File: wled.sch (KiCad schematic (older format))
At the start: 18 parts, among them J1 PROGRAM_HEADER, J2 LED0, J3 QWIIC, J4 POWER, Q1 S8050, Q2 S8050, U1 ESP-12F, U2 AMS1117-3.3

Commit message: fix 0603 components
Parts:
- C1, C2: footprint Capacitor_SMD:C_0201_0603Metric -> Capacitor_SMD:C_0603_1608Metric
- D2: footprint LED_SMD:LED_0201_0603Metric -> LED_SMD:LED_0603_1608Metric
- R1, R2: footprint Resistor_SMD:R_0201_0603Metric -> Resistor_SMD:R_0603_1608Metric
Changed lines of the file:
@@
 F 0 "R1" V 7493 2050 50  0000 C CNN
 F 1 "12k" V 7584 2050 50  0000 C CNN
-F 2 "Resistor_SMD:R_0201_0603Metric" V 7630 2050 50  0001 C CNN
+F 2 "Resistor_SMD:R_0603_1608Metric" V 7630 2050 50  0001 C CNN
 F 3 "~" H 7700 2050 50  0001 C CNN
 F 4 "C22790" H 7700 2050 50  0001 C CNN "JCSC"
@@
 F 0 "R2" V 7493 3200 50  0000 C CNN
 F 1 "12k" V 7584 3200 50  0000 C CNN
-F 2 "Resistor_SMD:R_0201_0603Metric" V 7630 3200 50  0001 C CNN
+F 2 "Resistor_SMD:R_0603_1608Metric" V 7630 3200 50  0001 C CNN
 F 3 "~" H 7700 3200 50  0001 C CNN
 F 4 "C22790" H 7700 3200 50  0001 C CNN "JCSC"
@@
 F 0 "C1" H 3815 4896 50  0000 L CNN
 F 1 "10uF" H 3815 4805 50  0000 L CNN
-F 2 "Capacitor_SMD:C_0201_0603Metric" H 3738 4700 50  0001 C CNN
+F 2 "Capacitor_SMD:C_0603_1608Metric" H 3738 4700 50  0001 C CNN
 F 3 "~" H 3700 4850 50  0001 C CNN
 F 4 "C19702" H 3700 4850 50  0001 C CNN "JCSC"
@@
 F 0 "C2" H 4765 4946 50  0000 L CNN
 F 1 "10uF" H 4765 4855 50  0000 L CNN
-F 2 "Capacitor_SMD:C_0201_0603Metric" H 4688 4750 50  0001 C CNN
+F 2 "Capacitor_SMD:C_0603_1608Metric" H 4688 4750 50  0001 C CNN
 F 3 "~" H 4650 4900 50  0001 C CNN
 F 4 "C19702" H 4650 4900 50  0001 C CNN "JCSC"
@@
 F 0 "D2" H 3443 5695 50  0000 C CNN
 F 1 "LED" H 3443 5786 50  0000 C CNN
-F 2 "LED_SMD:LED_0201_0603Metric" H 3450 5950 50  0001 C CNN
+F 2 "LED_SMD:LED_0603_1608Metric" H 3450 5950 50  0001 C CNN
 F 3 "~" H 3450 5950 50  0001 C CNN
 F 4 "C2286" H 3450 5950 50  0001 C CNN "JCSC"

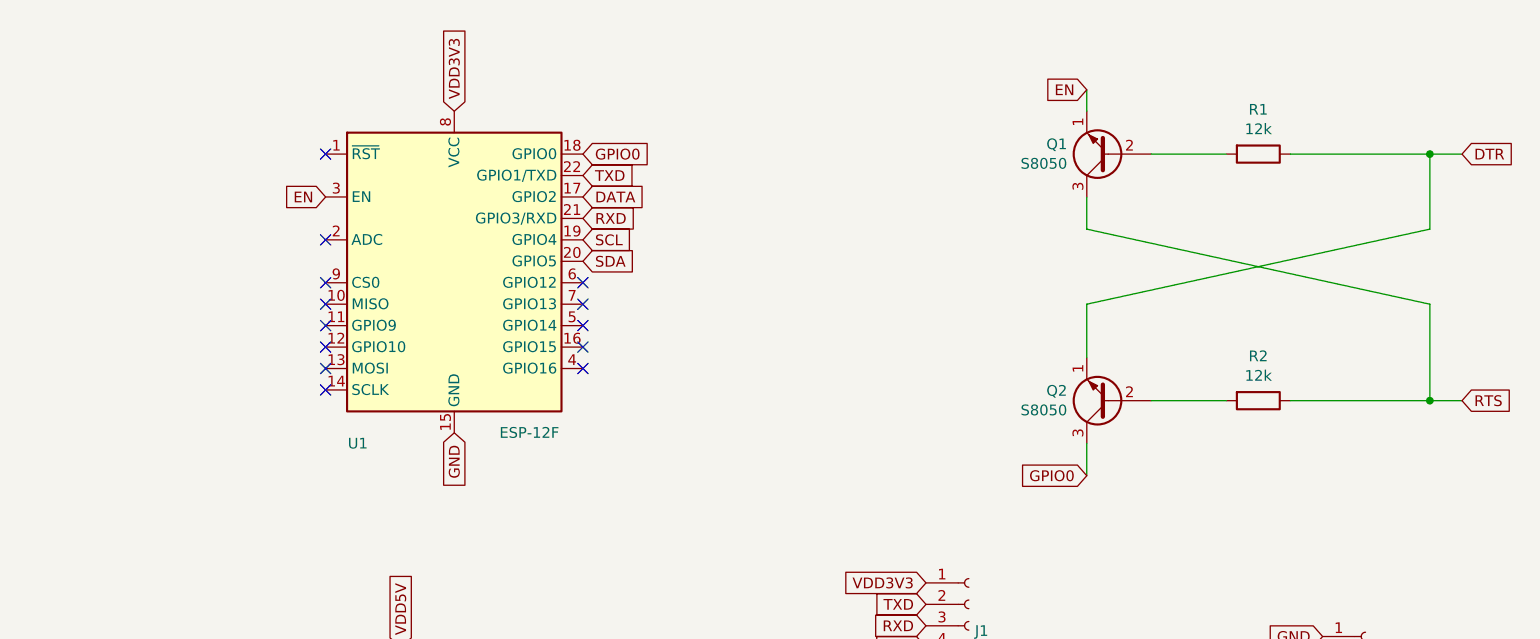
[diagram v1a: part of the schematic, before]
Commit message: updated parts/placements
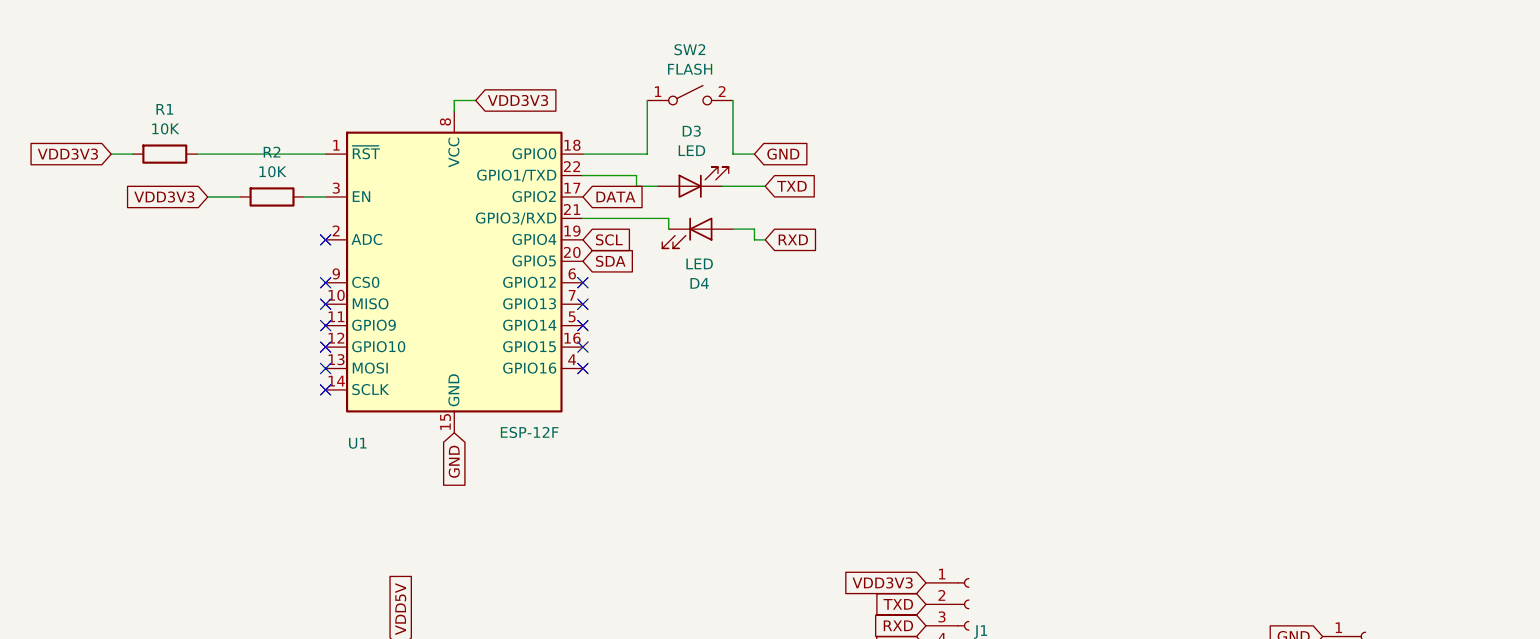
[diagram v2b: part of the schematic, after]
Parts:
- removed Q1, Q2: S8050, Package_TO_SOT_SMD:SOT-23, symbol Transistor_BJT:S8050
- added D3, D4: LED, LED_SMD:LED_0603_1608Metric, symbol Device:LED
- added SW2: FLASH, Button_Switch_SMD:SW_SPST_B3S-1000, symbol Switch:SW_SPST
- J1: footprint Connector_PinSocket_2.54mm:PinSocket_1x06_P2.54mm_Vertical -> Connector_JST:JST_XH_B6B-XH-A_1x06_P2.50mm_Vertical
- J4: footprint Connector_JST:JST_PH_B2B-PH-K_1x02_P2.00mm_Vertical -> Connector_JST:JST_XH_B2B-XH-A_1x02_P2.50mm_Vertical
- R1, R2: value 12k -> 10K; footprint Resistor_SMD:R_0603_1608Metric -> Resistor_SMD:R_0603_1608Metric_Pad0.98x0.95mm_HandSolder; JCSC C22790 -> (none); LCSC Part C22790 -> (none)
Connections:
- net DTR: no longer R1.1
- net GND: now also SW2.2 (B)
- net RTS: no longer R2.1
- net RXD: now also D4.2 (A); no longer U1.21 (GPIO3/RXD)
- net TXD: now also D3.1 (K); no longer U1.22 (GPIO1/TXD)
- net VDD3V3: now also R1.2, R2.2
- net at U1.1 (~RST): now also R1.1
- net EN: no longer names the net of U1.3 (EN)
- net EN: now also R2.1
- net GPIO0: no longer names the net of U1.18 (GPIO0)
- net GPIO0: now also SW2.1 (A)
- new net: D4.1 (K), U1.21 (GPIO3/RXD)
- new net: D3.2 (A), U1.22 (GPIO1/TXD)
- no-connect marks 13 -> 12
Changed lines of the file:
@@
 Comment4 ""
 $EndDescr
-$Comp
-L RF_Module:ESP-12F U1
-U 1 1 605E2E75
-P 3950 2650
-F 0 "U1" H 3500 1900 50  0000 C CNN
-F 1 "ESP-12F" H 4300 1950 50  0000 C CNN
-F 2 "RF_Module:ESP-12E" H 3950 2650 50  0001 C CNN
-F 3 "http://wiki.ai-thinker.com/_media/esp8266/esp8266_series_modules_user_manual_v1.1.pdf" H 3600 2750 50  0001 C CNN
-F 4 "C82891" H 3950 2650 50  0001 C CNN "JCSC"
-F 5 "C82891" H 3950 2650 50  0001 C CNN "LCSC Part"
-	1    3950 2650
-	1    0    0    -1
-$EndComp
-$Comp
-L Transistor_BJT:S8050 Q1
-U 1 1 605E3833
-P 7000 2050
-F 0 "Q1" H 7191 2004 50  0000 L CNN
-F 1 "S8050" H 7191 2095 50  0000 L CNN
-F 2 "Package_TO_SOT_SMD:SOT-23" H 7200 1975 50  0001 L CIN
-F 3 "http://www.unisonic.com.tw/datasheet/S8050.pdf" H 7000 2050 50  0001 L CNN
-F 4 "C2146" H 7000 2050 50  0001 C CNN "JCSC"
-F 5 "C2146" H 7000 2050 50  0001 C CNN "LCSC Part"
-	1    7000 2050
-	-1   0    0    1
-$EndComp
-$Comp
-L Transistor_BJT:S8050 Q2
-U 1 1 605E3CB7
-P 7000 3200
-F 0 "Q2" H 7191 3154 50  0000 L CNN
-F 1 "S8050" H 7191 3245 50  0000 L CNN
-F 2 "Package_TO_SOT_SMD:SOT-23" H 7200 3125 50  0001 L CIN
-F 3 "http://www.unisonic.com.tw/datasheet/S8050.pdf" H 7000 3200 50  0001 L CNN
-F 4 "C2146" H 7000 3200 50  0001 C CNN "JCSC"
-F 5 "C2146" H 7000 3200 50  0001 C CNN "LCSC Part"
-	1    7000 3200
-	-1   0    0    1
-$EndComp
-$Comp
-L Device:R R1
-U 1 1 605E460C
-P 7700 2050
-F 0 "R1" V 7493 2050 50  0000 C CNN
-F 1 "12k" V 7584 2050 50  0000 C CNN
-F 2 "Resistor_SMD:R_0603_1608Metric" V 7630 2050 50  0001 C CNN
-F 3 "~" H 7700 2050 50  0001 C CNN
-F 4 "C22790" H 7700 2050 50  0001 C CNN "JCSC"
-F 5 "C22790" H 7700 2050 50  0001 C CNN "LCSC Part"
-	1    7700 2050
-	0    1    1    0
-$EndComp
-$Comp
-L Device:R R2
-U 1 1 605E4B89
-P 7700 3200
-F 0 "R2" V 7493 3200 50  0000 C CNN
-F 1 "12k" V 7584 3200 50  0000 C CNN
-F 2 "Resistor_SMD:R_0603_1608Metric" V 7630 3200 50  0001 C CNN
-F 3 "~" H 7700 3200 50  0001 C CNN
-F 4 "C22790" H 7700 3200 50  0001 C CNN "JCSC"
-F 5 "C22790" H 7700 3200 50  0001 C CNN "LCSC Part"
-	1    7700 3200
-	0    1    1    0
-$EndComp
-Text GLabel 8650 2050 2    50   Input ~ 0
-DTR
-Text GLabel 8650 3200 2    50   Input ~ 0
-RTS
-Text GLabel 6900 3550 0    50   Input ~ 0
-GPIO0
-Text GLabel 6900 1750 0    50   Input ~ 0
-EN
-Wire Wire Line
-	7850 2050 8500 2050
-Wire Wire Line
-	8650 3200 8500 3200
-Wire Wire Line
-	6900 3000 6900 2750
-Wire Wire Line
-	6900 2750 8500 2400
-Wire Wire Line
-	8500 2400 8500 2050
-Connection ~ 8500 2050
-Wire Wire Line
-	8500 2050 8650 2050
-Wire Wire Line
-	8500 3200 8500 2750
-Wire Wire Line
-	8500 2750 6900 2400
-Wire Wire Line
-	6900 2400 6900 2250
-Connection ~ 8500 3200
-Wire Wire Line
-	8500 3200 7850 3200
-Wire Wire Line
-	6900 1850 6900 1750
-Wire Wire Line
-	7200 2050 7550 2050
-Wire Wire Line
-	6900 3550 6900 3400
-Wire Wire Line
-	7200 3200 7550 3200
-Text GLabel 4550 2050 2    50   Input ~ 0
-GPIO0
-Text GLabel 3350 2250 0    50   Input ~ 0
-EN
 Text GLabel 4550 2450 2    50   Input ~ 0
 SCL
@@
 F 0 "J4" H 8228 4826 50  0000 L CNN
 F 1 "POWER" H 8228 4735 50  0000 L CNN
-F 2 "Connector_JST:JST_PH_B2B-PH-K_1x02_P2.00mm_Vertical" H 8200 4850 50  0001 C CNN
+F 2 "Connector_JST:JST_XH_B2B-XH-A_1x02_P2.50mm_Vertical" H 8200 4850 50  0001 C CNN
 F 3 "~" H 8200 4850 50  0001 C CNN
 F 4 "0" H 8200 4850 50  0001 C CNN "JLCPCB BOM"
@@
 Text GLabel 3950 3350 3    50   Input ~ 0
 GND
-Text GLabel 3950 1850 1    50   Input ~ 0
+Text GLabel 4050 1800 2    50   Input ~ 0
 VDD3V3
 Text GLabel 4550 2250 2    50   Input ~ 0
 DATA
-Text GLabel 4550 2150 2    50   Input ~ 0
+Text GLabel 5400 2200 2    50   Input ~ 0
 TXD
-Text GLabel 4550 2350 2    50   Input ~ 0
+Text GLabel 5400 2450 2    50   Input ~ 0
 RXD
 $Comp
@@
 F 0 "J1" H 6378 4226 50  0000 L CNN
 F 1 "PROGRAM_HEADER" H 6378 4135 50  0000 L CNN
-F 2 "Connector_PinSocket_2.54mm:PinSocket_1x06_P2.54mm_Vertical" H 6350 4250 50  0001 C CNN
+F 2 "Connector_JST:JST_XH_B6B-XH-A_1x06_P2.50mm_Vertical" H 6350 4250 50  0001 C CNN
 F 3 "~" H 6350 4250 50  0001 C CNN
 F 4 "0" H 6350 4250 50  0001 C CNN "JLCPCB BOM"
@@
 NoConn ~ 3350 2650
 NoConn ~ 3350 2450
-NoConn ~ 3350 2050
 $Comp
 L Mechanical:MountingHole H1
@@
 	1    0    0    -1
 $EndComp
+$Comp
+L Switch:SW_SPST SW2
+U 1 1 60B01930
+P 5050 1800
+F 0 "SW2" H 5050 2035 50  0000 C CNN
+F 1 "FLASH" H 5050 1944 50  0000 C CNN
+F 2 "Button_Switch_SMD:SW_SPST_B3S-1000" H 5050 1800 50  0001 C CNN
+F 3 "~" H 5050 1800 50  0001 C CNN
+	1    5050 1800
+	1    0    0    -1
+$EndComp
+$Comp
+L Device:R R1
+U 1 1 60B03CF4
+P 2600 2050
+F 0 "R1" V 2393 2050 50  0000 C CNN
+F 1 "10K" V 2484 2050 50  0000 C CNN
+F 2 "Resistor_SMD:R_0603_1608Metric_Pad0.98x0.95mm_HandSolder" V 2530 2050 50  0001 C CNN
+F 3 "~" H 2600 2050 50  0001 C CNN
+	1    2600 2050
+	0    1    1    0
+$EndComp
+Text GLabel 2350 2050 0    50   Input ~ 0
+VDD3V3
+Wire Wire Line
+	2450 2050 2350 2050
+$Comp
+L Device:R R2
+U 1 1 60B0901B
+P 3100 2250
+F 0 "R2" V 2893 2250 50  0000 C CNN
+F 1 "10K" V 2984 2250 50  0000 C CNN
+F 2 "Resistor_SMD:R_0603_1608Metric_Pad0.98x0.95mm_HandSolder" V 3030 2250 50  0001 C CNN
+F 3 "~" H 3100 2250 50  0001 C CNN
+	1    3100 2250
+	0    1    1    0
+$EndComp
+Text GLabel 2800 2250 0    50   Input ~ 0
+VDD3V3
+Wire Wire Line
+	3250 2250 3350 2250
+Wire Wire Line
+	2800 2250 2950 2250
+Wire Wire Line
+	4050 1800 3950 1800
+Wire Wire Line
+	3950 1800 3950 1850
+Text GLabel 5350 2050 2    50   Input ~ 0
+GND
+Wire Wire Line
+	5250 2050 5350 2050
+Wire Wire Line
+	4850 2050 4550 2050
+$Comp
+L Device:LED D4
+U 1 1 60B0CA21
+P 5100 2400
+F 0 "D4" H 5093 2145 50  0000 C CNN
+F 1 "LED" H 5093 2236 50  0000 C CNN
+F 2 "LED_SMD:LED_0603_1608Metric" H 5100 2400 50  0001 C CNN
+F 3 "~" H 5100 2400 50  0001 C CNN
+F 4 "C2286" H 5100 2400 50  0001 C CNN "JCSC"
+F 5 "C2286" H 5100 2400 50  0001 C CNN "LCSC Part"
+	1    5100 2400
+	1    0    0    -1
+$EndComp
+$Comp
+L Device:LED D3
+U 1 1 60B0E01C
+P 5050 2200
+F 0 "D3" H 5043 1945 50  0000 C CNN
+F 1 "LED" H 5043 2036 50  0000 C CNN
+F 2 "LED_SMD:LED_0603_1608Metric" H 5050 2200 50  0001 C CNN
+F 3 "~" H 5050 2200 50  0001 C CNN
+F 4 "C2286" H 5050 2200 50  0001 C CNN "JCSC"
+F 5 "C2286" H 5050 2200 50  0001 C CNN "LCSC Part"
+	1    5050 2200
+	-1   0    0    1
+$EndComp
+Wire Wire Line
+	5400 2200 5200 2200
+Wire Wire Line
+	4900 2200 4800 2200
+Wire Wire Line
+	4800 2200 4800 2150
+Wire Wire Line
+	4800 2150 4550 2150
+Wire Wire Line
+	4550 2350 4950 2350
+Wire Wire Line
+	4950 2350 4950 2400
+Wire Wire Line
+	5250 2400 5350 2400
+Wire Wire Line
+	5350 2400 5350 2450
+Wire Wire Line
+	5350 2450 5400 2450
+Wire Wire Line
+	4850 2050 4850 1800
+Wire Wire Line
+	5250 2050 5250 1800
+$Comp
+L RF_Module:ESP-12F U1
+U 1 1 605E2E75
+P 3950 2650
+F 0 "U1" H 3500 1900 50  0000 C CNN
+F 1 "ESP-12F" H 4300 1950 50  0000 C CNN
+F 2 "RF_Module:ESP-12E" H 3950 2650 50  0001 C CNN
+F 3 "http://wiki.ai-thinker.com/_media/esp8266/esp8266_series_modules_user_manual_v1.1.pdf" H 3600 2750 50  0001 C CNN
+F 4 "C82891" H 3950 2650 50  0001 C CNN "JCSC"
+F 5 "C82891" H 3950 2650 50  0001 C CNN "LCSC Part"
+	1    3950 2650
+	1    0    0    -1
+$EndComp
+Wire Wire Line
+	2750 2050 3350 2050
 $EndSCHEMATC

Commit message: forgot to save schematic
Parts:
- added R3, R5: 250, Resistor_SMD:R_0603_1608Metric_Pad0.98x0.95mm_HandSolder, symbol Device:R
- added R4: 10K, Resistor_SMD:R_0603_1608Metric_Pad0.98x0.95mm_HandSolder, symbol Device:R
- added SW1: RESET, Button_Switch_SMD:SW_SPST_B3S-1000, symbol Switch:SW_SPST
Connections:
- net GND: now also D3.1 (K), D4.1 (K), SW1.2 (B)
- net RXD: now also U1.21 (GPIO3/RXD), R5.2; no longer D4.2 (A)
- net TXD: now also U1.22 (GPIO1/TXD), R4.1; no longer D3.1 (K)
- net VDD3V3: now also R3.1
- net VDD5V: no longer D2.2 (A)
- net at R1.1, U1.1 (~RST): now also SW1.1 (A)
- net at D3.2 (A): now also R4.2; no longer U1.22 (GPIO1/TXD)
- new net: D2.2 (A), R3.2
- new net: D4.2 (A), R5.1
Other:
- moved on the sheet: D3, D4, SW2
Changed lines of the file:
@@
 Wire Wire Line
 	3700 4600 3700 4350
-Text GLabel 3150 5950 0    50   Input ~ 0
-VDD5V
+Text GLabel 2700 5950 0    50   Input ~ 0
+VDD3V3
 $Comp
 L Device:LED D2
@@
 Wire Wire Line
 	3700 5950 3600 5950
-Wire Wire Line
-	3300 5950 3150 5950
 $Comp
 L Connector:Conn_01x04_Female J3
@@
 L Switch:SW_SPST SW2
 U 1 1 60B01930
-P 5050 1800
-F 0 "SW2" H 5050 2035 50  0000 C CNN
-F 1 "FLASH" H 5050 1944 50  0000 C CNN
-F 2 "Button_Switch_SMD:SW_SPST_B3S-1000" H 5050 1800 50  0001 C CNN
-F 3 "~" H 5050 1800 50  0001 C CNN
-	1    5050 1800
+P 5050 950
+F 0 "SW2" H 5050 1185 50  0000 C CNN
+F 1 "FLASH" H 5050 1094 50  0000 C CNN
+F 2 "Button_Switch_SMD:SW_SPST_B3S-1000" H 5050 950 50  0001 C CNN
+F 3 "~" H 5050 950 50  0001 C CNN
+	1    5050 950
 	1    0    0    -1
 $EndComp
@@
 L Device:LED D4
 U 1 1 60B0CA21
-P 5100 2400
-F 0 "D4" H 5093 2145 50  0000 C CNN
-F 1 "LED" H 5093 2236 50  0000 C CNN
-F 2 "LED_SMD:LED_0603_1608Metric" H 5100 2400 50  0001 C CNN
-F 3 "~" H 5100 2400 50  0001 C CNN
-F 4 "C2286" H 5100 2400 50  0001 C CNN "JCSC"
-F 5 "C2286" H 5100 2400 50  0001 C CNN "LCSC Part"
-	1    5100 2400
-	1    0    0    -1
+P 5100 3050
+F 0 "D4" H 5093 2795 50  0000 C CNN
+F 1 "LED" H 5093 2886 50  0000 C CNN
+F 2 "LED_SMD:LED_0603_1608Metric" H 5100 3050 50  0001 C CNN
+F 3 "~" H 5100 3050 50  0001 C CNN
+F 4 "C2286" H 5100 3050 50  0001 C CNN "JCSC"
+F 5 "C2286" H 5100 3050 50  0001 C CNN "LCSC Part"
+	1    5100 3050
+	0    -1   -1   0
 $EndComp
 $Comp
 L Device:LED D3
 U 1 1 60B0E01C
-P 5050 2200
-F 0 "D3" H 5043 1945 50  0000 C CNN
-F 1 "LED" H 5043 2036 50  0000 C CNN
-F 2 "LED_SMD:LED_0603_1608Metric" H 5050 2200 50  0001 C CNN
-F 3 "~" H 5050 2200 50  0001 C CNN
-F 4 "C2286" H 5050 2200 50  0001 C CNN "JCSC"
-F 5 "C2286" H 5050 2200 50  0001 C CNN "LCSC Part"
-	1    5050 2200
-	-1   0    0    1
-$EndComp
-Wire Wire Line
-	5400 2200 5200 2200
-Wire Wire Line
-	4900 2200 4800 2200
+P 5050 1550
+F 0 "D3" H 5043 1295 50  0000 C CNN
+F 1 "LED" H 5043 1386 50  0000 C CNN
+F 2 "LED_SMD:LED_0603_1608Metric" H 5050 1550 50  0001 C CNN
+F 3 "~" H 5050 1550 50  0001 C CNN
+F 4 "C2286" H 5050 1550 50  0001 C CNN "JCSC"
+F 5 "C2286" H 5050 1550 50  0001 C CNN "LCSC Part"
+	1    5050 1550
+	0    1    1    0
+$EndComp
 Wire Wire Line
 	4800 2200 4800 2150
@@
 	4950 2350 4950 2400
 Wire Wire Line
-	5250 2400 5350 2400
-Wire Wire Line
 	5350 2400 5350 2450
 Wire Wire Line
 	5350 2450 5400 2450
 Wire Wire Line
-	4850 2050 4850 1800
-Wire Wire Line
-	5250 2050 5250 1800
+	4850 2050 4850 950
+Wire Wire Line
+	5250 2050 5250 950
 $Comp
 L RF_Module:ESP-12F U1
@@
 $EndComp
 Wire Wire Line
-	2750 2050 3350 2050
+	2750 2050 3050 2050
+Text GLabel 5050 1250 1    50   Input ~ 0
+GND
+Text GLabel 5100 3300 3    50   Input ~ 0
+GND
+Wire Wire Line
+	5100 3200 5100 3300
+Wire Wire Line
+	5050 1400 5050 1250
+Wire Wire Line
+	4950 2400 5100 2400
+$Comp
+L Device:R R5
+U 1 1 60C05B3D
+P 5100 2600
+F 0 "R5" V 4893 2600 50  0000 C CNN
+F 1 "250" V 4984 2600 50  0000 C CNN
+F 2 "Resistor_SMD:R_0603_1608Metric_Pad0.98x0.95mm_HandSolder" V 5030 2600 50  0001 C CNN
+F 3 "~" H 5100 2600 50  0001 C CNN
+	1    5100 2600
+	-1   0    0    1
+$EndComp
+Wire Wire Line
+	4800 2200 5050 2200
+Wire Wire Line
+	5050 2200 5050 2100
+Connection ~ 5050 2200
+Wire Wire Line
+	5050 2200 5400 2200
+Wire Wire Line
+	5050 1800 5050 1700
+Wire Wire Line
+	5100 2900 5100 2750
+Wire Wire Line
+	5100 2450 5100 2400
+Connection ~ 5100 2400
+Wire Wire Line
+	5100 2400 5350 2400
+$Comp
+L Device:R R4
+U 1 1 60C081D0
+P 5050 1950
+F 0 "R4" V 4843 1950 50  0000 C CNN
+F 1 "10K" V 4934 1950 50  0000 C CNN
+F 2 "Resistor_SMD:R_0603_1608Metric_Pad0.98x0.95mm_HandSolder" V 4980 1950 50  0001 C CNN
+F 3 "~" H 5050 1950 50  0001 C CNN
+	1    5050 1950
+	-1   0    0    1
+$EndComp
+$Comp
+L Device:R R3
+U 1 1 60C0A230
+P 2950 5950
+F 0 "R3" V 2743 5950 50  0000 C CNN
+F 1 "250" V 2834 5950 50  0000 C CNN
+F 2 "Resistor_SMD:R_0603_1608Metric_Pad0.98x0.95mm_HandSolder" V 2880 5950 50  0001 C CNN
+F 3 "~" H 2950 5950 50  0001 C CNN
+	1    2950 5950
+	0    -1   -1   0
+$EndComp
+Wire Wire Line
+	3100 5950 3300 5950
+Wire Wire Line
+	2800 5950 2700 5950
+Text GLabel 3050 1150 1    50   Input ~ 0
+GND
+Wire Wire Line
+	3050 2050 3050 1850
+Connection ~ 3050 2050
+Wire Wire Line
+	3050 2050 3350 2050
+Wire Wire Line
+	3050 1450 3050 1150
+$Comp
+L Switch:SW_SPST SW1
+U 1 1 60C0B809
+P 3050 1650
+F 0 "SW1" H 3050 1885 50  0000 C CNN
+F 1 "RESET" H 3050 1794 50  0000 C CNN
+F 2 "Button_Switch_SMD:SW_SPST_B3S-1000" H 3050 1650 50  0001 C CNN
+F 3 "~" H 3050 1650 50  0001 C CNN
+	1    3050 1650
+	0    -1   -1   0
+$EndComp
 $EndSCHEMATC

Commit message: update schem
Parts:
- removed C1, C2: 10uF, Capacitor_SMD:C_0603_1608Metric, symbol Device:C
- removed D1: 1N5819, Diode_SMD:D_SOD-323, symbol Diode:1N5819
- removed D3, D4: LED, LED_SMD:LED_0603_1608Metric, symbol Device:LED
- removed J1: PROGRAM_HEADER, Connector_JST:JST_XH_B6B-XH-A_1x06_P2.50mm_Vertical, symbol Connector:Conn_01x06_Female
- removed J2: LED0, Connector_PinHeader_2.54mm:PinHeader_1x03_P2.54mm_Vertical, symbol Connector:Conn_01x03_Female
- removed R2, R4: 10K, Resistor_SMD:R_0603_1608Metric_Pad0.98x0.95mm_HandSolder, symbol Device:R
- removed R5: 250, Resistor_SMD:R_0603_1608Metric_Pad0.98x0.95mm_HandSolder, symbol Device:R
- removed SW2: FLASH, Button_Switch_SMD:SW_SPST_B3S-1000, symbol Switch:SW_SPST
- removed U2: AMS1117-3.3, Package_TO_SOT_SMD:SOT-223-3_TabPin2, symbol Regulator_Linear:AMS1117-3.3
- added D? (x2): LED, LED_SMD:LED_0603_1608Metric, symbol Device:LED
- added J?: USB_B_Micro, symbol Connector:USB_B_Micro
- added Q? (x2): BC817, Package_TO_SOT_SMD:SOT-23, symbol Transistor_BJT:BC817
- added R? (x4): 10K, Resistor_SMD:R_0603_1608Metric_Pad0.98x0.95mm_HandSolder, symbol Device:R
- added R? (x2): 250, Resistor_SMD:R_0603_1608Metric_Pad0.98x0.95mm_HandSolder, symbol Device:R
- added U?: CP2102N-A01-GQFN28, Package_DFN_QFN:QFN-28-1EP_5x5mm_P0.5mm_EP3.35x3.35mm, symbol Interface_USB:CP2102N-A01-GQFN28
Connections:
- net DTR: now also Q?.2 (E), R?.1, U?.28 (~DTR)
- net GND: now also D?.1 (K), D?.1 (K), J?.5 (GND), J?.6 (Shield), R?.1, U?.29 (GND), U?.3 (GND)
- net RTS: now also Q?.2 (E), R?.1, U?.24 (~RTS)
- net RXD: now also R?.1, U?.26 (TXD)
- net TXD: now also R?.1, U?.25 (RXD)
- net VDD3V3: now also R?.2, U?.6 (VDD)
- net VIN: now also U?.7 (REGIN)
- net RST: now reaches R1.1, SW1.1 (A)
- net RST: no longer U1.1 (~RST)
- net at U1.16 (GPIO15): now also R?.2
- net GPIO0: now reaches U1.18 (GPIO0)
- net GPIO0: now also Q?.3 (C)
- net at U1.3 (EN): now also R?.1
- new net: J?.3 (D+), U?.4 (D+)
- new net: J?.2 (D-), U?.5 (D-)
- new net: J?.1 (VBUS), U?.8 (VBUS)
- new net: Q?.1 (B), R?.2 (x2)
- new net: D?.2 (A), R?.2 (x2)
- new net EN: Q?.3 (C)
- no-connect marks 12 -> 23
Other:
- moved on the sheet: R1, SW1
